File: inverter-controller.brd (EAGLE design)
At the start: 18.5 x 86.8 mm, 140 parts, among them IC1 STM32F334C8T6, IC2 SY7152ABC, IC3 LMV358MMX, IC4 LMV358MMX, IC5 SY7152ABC, J1 621006245821, J2 61300211121, X1 0289-9066**15EDGVC-3.81-02P-14, X2 0289-9066**15EDGVC-3.81-02P-14, X4 0289-9066**15EDGVC-3.81-02P-14, X6 1365-16, Y1 NX2016SA-32M

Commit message: Direnc ve kondansator kutuphaneleri degistirildi(silk sorunu nedeniyle).
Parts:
- removed C58: 100n, rcl:C0603
- removed LED10, LED7, LED9: (no value), adafruit:CHIPLED_0805
- removed R51, R52, R62, R63, R64: 33R, rcl:R0603
- removed R53, R54, R65, R66: 1k, rcl:R0603
- removed R55, R76: 470R, rcl:R0603
- removed R56: 220R, rcl:R0603
- removed R57: 1M, rcl:R0603
- removed R58: 200k, rcl:R0603
- removed R59: 10.5k, rcl:R0603
- removed R60, R61: 0R, rcl:R0603
- removed R71, R75: NC, rcl:R0603
- added C20: 10nF, rcl:C0603_ENKO
- added LED1, LED2, LED3: (no value), adafruit:CHIP-LED0805
- added R16: 220R, rcl:R0603_ENKO
- added R36, R37: 470R, rcl:R0603_ENKO
- added R38, R39, R47: 33R, rcl:R0603_ENKO
- added R40, R44: 1K, rcl:R0603_ENKO
- added R41: 1M, rcl:R0603_ENKO
- added R42: 200K, rcl:R0603_ENKO
- added R43: 10.5K, rcl:R0603_ENKO
- added R45, R46: 0R, rcl:R0603_ENKO
- C1, C2: value (none) -> 10pF; device rcl:C0603 -> rcl:C0603_ENKO
- C10, C13, C19, C37, C38, C47: value 100n -> 100nF; device rcl:C0603 -> rcl:C0603_ENKO
- C11: value 4.7u -> 4.7uF; device rcl:C0603 -> rcl:C0603_ENKO
- C12: value 1019-3366**CAP 0603 CER 10uF 16V %20 X5R -> 10uF; device rcl:C0603 -> rcl:C0603_ENKO
- C14, C3, C39, C48, C5, C52, C57: value 10n -> 10nF; device rcl:C0603 -> rcl:C0603_ENKO
- C15, C16, C54: value 10u -> 10uF; device rcl:C0805 -> rcl:C0603_ENKO
- C17, C22, C24, C26, C28, C30, C32, C34, C42, C45, C51: value 100n -> 10nF; device rcl:C0603 -> rcl:C0603_ENKO
- C18, C21, C23, C25, C27, C29, C31, C33, C35, C43, C46, C56: value 10n -> 100nF; device rcl:C0603 -> rcl:C0603_ENKO
- C36: value 100n -> 120pF; device rcl:C0603 -> rcl:C0603_ENKO
- C4: value 1u -> 1uF; device rcl:C0603 -> rcl:C0603_ENKO
- C40: value 120p -> 100nF; device rcl:C0603 -> rcl:C0603_ENKO
- C41, C44: value 120p -> 120pF; device rcl:C0603 -> rcl:C0603_ENKO
- C49, C55: value 100n -> 10uF; device rcl:C0603 -> rcl:C0603_ENKO
- C50: value 1019-3366**CAP 0603 CER 10uF 16V %20 X5R -> 100nF; device rcl:C0603 -> rcl:C0603_ENKO
- C53: value 10u -> 100nF; device rcl:C0805 -> rcl:C0603_ENKO
- C6, C8: value 100n -> 4.7uF; device rcl:C0603 -> rcl:C0603_ENKO
- C7, C9: value 4.7u -> 100nF; device rcl:C0603 -> rcl:C0603_ENKO
- R1, R32: value (none) -> 1K; device rcl:R0603 -> rcl:R0603_ENKO
- R10, R11, R12, R13, R14, R15, R17, R18, R19, R2, R20, R21, R22, R23, R24, R25, R26, R27, R28, R29, R30, R31, R4, R7, R8, R9: device rcl:R0603 -> rcl:R0603_ENKO
- R3: value 10k -> 10K; device rcl:R0603 -> rcl:R0603_ENKO
- R33, R34: value (none) -> 0R; device rcl:R0603 -> rcl:R0603_ENKO
- R35: value (none) -> 33R; device rcl:R0603 -> rcl:R0603_ENKO
- R48, R49: value 0R -> 33R; device rcl:R0603 -> rcl:R0603_ENKO
- R5: value 200k -> 200K; device rcl:R0603 -> rcl:R0603_ENKO
- R50: value 33R -> 1K; device rcl:R0603 -> rcl:R0603_ENKO
- R6: value 10.5k -> 10.5K; device rcl:R0603 -> rcl:R0603_ENKO
- moved R50 653.0 mm to (-144.2, -544.9)
- moved C57 652.1 mm to (-144.2, -554.9)
- moved R49 648.8 mm to (-144.2, -539.9)
- moved C56 647.4 mm to (-144.2, -549.9)
- moved R48 644.7 mm to (-144.2, -534.9)
- moved C55 604.1 mm to (-138.1, -510.0)
- moved C52 592.6 mm to (-138.1, -495.0)
- moved C54 580.2 mm to (-138.1, -505.0)
- moved C53 576.0 mm to (-138.1, -500.0)
- moved C51 570.0 mm to (-138.1, -475.0)
- moved C49 560.8 mm to (-138.1, -465.1)
- moved C48 558.0 mm to (-138.1, -460.1)
- moved R35 555.8 mm to (-138.1, -435.1)
- moved R32 552.0 mm to (-131.9, -430.1)
- moved C47 551.7 mm to (-138.1, -455.1)
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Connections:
- removed net HRTIM1_CHA1: IC1.29, R17.1
- removed net HRTIM1_CHA2: IC1.30, R18.1
- removed net HRTIM1_CHB1: IC1.31, R19.1
- removed net HRTIM1_CHB2: IC1.32, R20.1
- removed net N$39: LED9.A, R56.2
- removed net N$48: C12.1, C13.1, C14.1, IC2.5, L4.1, R71.2
- removed net N$51: C50.1, C51.1, C52.1, IC5.5, L1.1, R75.2
- new net N$22: LED1.A, R16.2
- net +12V/1: now also R32.1, R33.2, R34.2, R5.1; no longer R48.2, R49.2, R5.2, R54.1
- net +12V/2: now also C52.1, R42.1, R44.1, R45.2, R46.2; no longer C56.1, R58.2, R60.2, R61.2, R66.1
- net +3V3: now also C12.1, C13.1, C14.1, C46.1, C49.1, C50.1, C51.1, C6.1, C7.1, IC2.5, IC5.5, L1.1, L4.1, R16.1, R18.1, R36.1, R37.1; no longer C47.1, C6.2, C7.2, R33.1, R55.1, R56.1, R71.1, R75.1, R76.1
- net FAN2_EN: now also R41.2; no longer R57.2
- net G11_PWM: now also IC1.29; no longer R17.2
- net G12_PWM: now also IC1.30; no longer R18.2
- net G13_PWM: now also IC1.31; no longer R19.2
- net G14_PWM: now also IC1.32; no longer R20.2
- net GND: now also C19.1, C20.2, C40.2, C6.2, C7.2, LED1.C, LED2.C, LED3.C, R19.2, R24.2, R29.2, R35.2, R38.2, R39.2, R41.1, R43.2, R47.2, R48.2, R49.2, R6.2, R7.2; no longer C19.2, C36.2, C58.2, C6.1, C7.1, LED10.C, LED7.C, LED9.C, R24.1, R29.1, R34.1, R50.2, R51.2, R52.2, R57.1, R59.1, R6.1, R62.2, R63.2, R64.2, R7.1
- net IA: now also C26.1, R17.1; no longer C28.1, R21.1
- net IB: now also C30.1, R22.1; no longer C32.1, R27.1
- net IIN_SENS: now also R8.2; no longer R8.1
- net I_FAN: now also C47.1, C56.1, R40.2, R50.2; no longer C49.1, C58.1, R53.2, R65.2
- net I_IN: now also C34.1, R27.1, R8.1; no longer C36.1, R32.1, R8.2
- net N$1: now also C36.2, R20.1, R21.2; no longer C40.2, R22.2, R25.1
- net N$10: now also R35.1, R38.1, R39.1, R40.1; no longer R50.1, R51.1, R52.1, R53.1
- net N$13: now also R20.2; no longer R25.2
- net N$14: now also C42.1, R26.2; no longer C43.1, R30.2
- net N$15: now also R18.2, R19.1; no longer R23.2, R24.2
- net N$16: now also R22.2, R25.1; no longer R26.1, R27.2
- net N$17: now also R27.2, R30.1; no longer R31.1, R32.2
- net N$18: now also C40.1, R23.2, R24.1; no longer C42.1, R28.2, R29.2
- net N$19: now also R25.2, R26.1; no longer R26.2, R30.1
- net N$20: now also C45.1, R31.2; no longer C46.1, R35.2
- net N$21: now also C43.1, R28.2, R29.1; no longer C45.1, R33.2, R34.2
- net N$23: now also R30.2, R31.1; no longer R31.2, R35.1
- net N$34: now also R33.1, R34.1; no longer R48.1, R49.1
- net N$35: now also R36.2; no longer R76.2
- net N$40: now also R42.2, R43.1; no longer R58.1, R59.2
- net N$41: now also R45.1, R46.1; no longer R60.1, R61.1
- net N$42: now also R47.1, R48.1, R49.1, R50.1; no longer R62.1, R63.1, R64.1, R65.1
- net N$43: now also LED3.A, R44.2; no longer LED10.A, R66.2
- net N$47: now also R37.2; no longer R55.2
- net N$7: now also C36.1, R17.2, R21.1; no longer C40.1, R21.2, R22.1
- net N$8: now also R5.2, R6.1; no longer R5.1, R6.2
- net N$9: now also LED2.A, R32.2; no longer LED7.A, R54.2
- net NTC1: now also C19.2, R7.1; no longer C19.1, R7.2
- net VA: now also C24.1; no longer C26.1
- net VB: now also C28.1; no longer C30.1
- net VIN_1: now also C20.1; no longer C22.1
- net VIN_2: now also C32.1; no longer C34.1
- net VOUT: now also C22.1; no longer C24.1
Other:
- board size 18.5 x 86.8 mm -> 52 x 37.6 mm

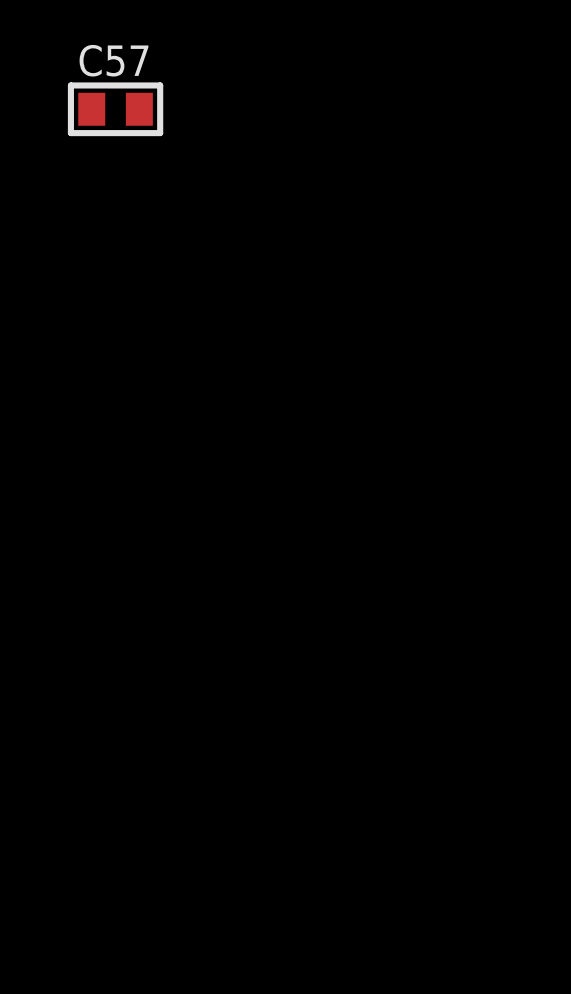
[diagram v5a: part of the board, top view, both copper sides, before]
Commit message: Akim olcumleri icin gerilim bolucu direncler eklendi.
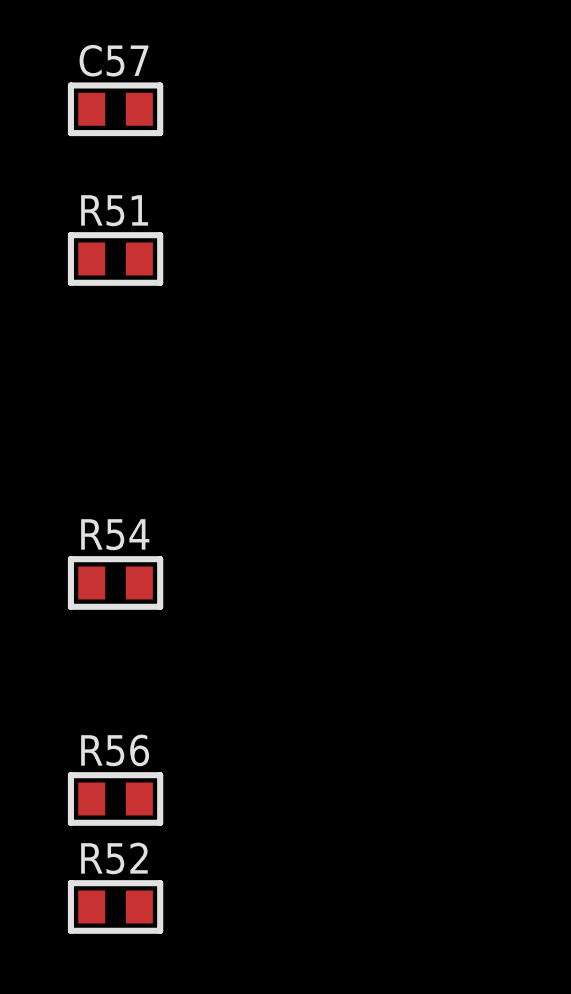
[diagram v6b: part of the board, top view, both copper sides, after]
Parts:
- added R51, R52, R54, R56: (no value), rcl:R0603_ENKO
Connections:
- net GND: now also R51.1, R52.1, R54.1, R56.1
- net IA: now also R54.2
- net IB: now also R56.2
- net I_IN: now also R52.2
- net VIN_1: now also R51.2
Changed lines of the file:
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@@
 <attribute name="VALUE" x="-145.5" y="-556.775" size="0.8128" layer="27" ratio="10"/>
+</element>
+<element name="R51" library="rcl" library_urn="urn:adsk.eagle:library:26637914" package="R0603_ENKO" package3d_urn="urn:adsk.eagle:package:26638826/1" value="" x="-144.23" y="-559.86" smashed="yes">
+<attribute name="NAME" x="-145.5" y="-558.7487" size="1.016" layer="25" ratio="18"/>
+<attribute name="VALUE" x="-145.5" y="-561.765" size="0.8128" layer="27" ratio="10"/>
+</element>
+<element name="R54" library="rcl" library_urn="urn:adsk.eagle:library:26637914" package="R0603_ENKO" package3d_urn="urn:adsk.eagle:package:26638826/1" value="" x="-144.23" y="-570.66" smashed="yes">
+<attribute name="NAME" x="-145.5" y="-569.5487" size="1.016" layer="25" ratio="18"/>
+<attribute name="VALUE" x="-145.5" y="-572.565" size="0.8128" layer="27" ratio="10"/>
+</element>
+<element name="R56" library="rcl" library_urn="urn:adsk.eagle:library:26637914" package="R0603_ENKO" package3d_urn="urn:adsk.eagle:package:26638826/1" value="" x="-144.23" y="-577.86" smashed="yes">
+<attribute name="NAME" x="-145.5" y="-576.7487" size="1.016" layer="25" ratio="18"/>
+<attribute name="VALUE" x="-145.5" y="-579.765" size="0.8128" layer="27" ratio="10"/>
+</element>
+<element name="R52" library="rcl" library_urn="urn:adsk.eagle:library:26637914" package="R0603_ENKO" package3d_urn="urn:adsk.eagle:package:26638826/1" value="" x="-144.23" y="-581.46" smashed="yes">
+<attribute name="NAME" x="-145.5" y="-580.3487" size="1.016" layer="25" ratio="18"/>
+<attribute name="VALUE" x="-145.5" y="-583.365" size="0.8128" layer="27" ratio="10"/>
 </element>
 </elements>
@@
 <contactref element="R11" pad="2"/>
 <contactref element="R17" pad="1"/>
+<contactref element="R54" pad="2"/>
 <wire x1="-126.5738" y1="-87.02" x2="-126.5738" y2="-92.01" width="0" layer="19" extent="1-1"/>
 <wire x1="-124.9862" y1="-134.14" x2="-126.5738" y2="-92.01" width="0" layer="19" extent="1-1"/>
 <wire x1="-132.7238" y1="-249.16" x2="-124.9862" y2="-134.14" width="0" layer="19" extent="1-1"/>
 <wire x1="36.26" y1="41.148" x2="-126.5738" y2="-87.02" width="0" layer="19" extent="1-16"/>
+<wire x1="-143.4362" y1="-570.66" x2="-132.7238" y2="-249.16" width="0" layer="19" extent="1-1"/>
 </signal>
 <signal name="IB">
@@
 <contactref element="R9" pad="2"/>
 <contactref element="R22" pad="1"/>
+<contactref element="R56" pad="2"/>
 <wire x1="-126.5738" y1="-111.97" x2="-124.9862" y2="-126.94" width="0" layer="19" extent="1-1"/>
 <wire x1="-126.5738" y1="-106.98" x2="-126.5738" y2="-111.97" width="0" layer="19" extent="1-1"/>
 <wire x1="-132.7238" y1="-287.12" x2="-124.9862" y2="-126.94" width="0" layer="19" extent="1-1"/>
 <wire x1="39.748" y1="39.66" x2="-126.5738" y2="-106.98" width="0" layer="19" extent="1-16"/>
+<wire x1="-143.4362" y1="-577.86" x2="-132.7238" y2="-287.12" width="0" layer="19" extent="1-1"/>
 </signal>
 <signal name="VIN_1">
@@
 <contactref element="C21" pad="1"/>
 <contactref element="R14" pad="2"/>
+<contactref element="R51" pad="2"/>
+<wire x1="-124.9862" y1="-144.94" x2="-143.4362" y2="-559.86" width="0" layer="19" extent="1-1"/>
+<wire x1="-126.5738" y1="-67.63" x2="-124.9862" y2="-144.94" width="0" layer="19" extent="1-1"/>
 <wire x1="-126.5738" y1="-64.03" x2="-126.5738" y2="-67.63" width="0" layer="19" extent="1-1"/>
-<wire x1="-124.9862" y1="-144.94" x2="-126.5738" y2="-67.63" width="0" layer="19" extent="1-1"/>
 <wire x1="39.748" y1="38.66" x2="-126.5738" y2="-64.03" width="0" layer="19" extent="1-16"/>
 </signal>
@@
 <contactref element="C35" pad="1"/>
 <contactref element="R27" pad="1"/>
+<contactref element="R52" pad="2"/>
+<wire x1="-132.7238" y1="-320.09" x2="-143.4362" y2="-581.46" width="0" layer="19" extent="1-1"/>
 <wire x1="-126.5738" y1="-165.72" x2="-132.7238" y2="-320.09" width="0" layer="19" extent="1-1"/>
 <wire x1="-126.5738" y1="-160.73" x2="-126.5738" y2="-165.72" width="0" layer="19" extent="1-1"/>
@@
 <contactref element="C56" pad="2"/>
 <contactref element="C57" pad="2"/>
+<contactref element="R51" pad="1"/>
+<contactref element="R54" pad="1"/>
+<contactref element="R56" pad="1"/>
+<contactref element="R52" pad="1"/>
 <wire x1="-131.1362" y1="-371.63" x2="-131.1362" y2="-376.62" width="0" layer="19" extent="1-1"/>
 <wire x1="-131.1362" y1="-366.64" x2="-131.1362" y2="-371.63" width="0" layer="19" extent="1-1"/>
@@
 <wire x1="-143.4362" y1="-549.88" x2="-143.4362" y2="-539.9" width="0" layer="19" extent="1-1"/>
 <wire x1="-143.4362" y1="-554.87" x2="-143.4362" y2="-549.88" width="0" layer="19" extent="1-1"/>
+<wire x1="-145.0238" y1="-559.86" x2="-143.4362" y2="-554.87" width="0" layer="19" extent="1-1"/>
+<wire x1="-145.0238" y1="-570.66" x2="-145.0238" y2="-559.86" width="0" layer="19" extent="1-1"/>
+<wire x1="-145.0238" y1="-577.86" x2="-145.0238" y2="-570.66" width="0" layer="19" extent="1-1"/>
+<wire x1="-145.0238" y1="-581.46" x2="-145.0238" y2="-577.86" width="0" layer="19" extent="1-1"/>
 <wire x1="-124.9862" y1="-165.72" x2="-132.7238" y2="-184.29" width="0" layer="19" extent="1-1"/>
 <wire x1="-124.9862" y1="-160.73" x2="-124.9862" y2="-165.72" width="0" layer="19" extent="1-1"/>

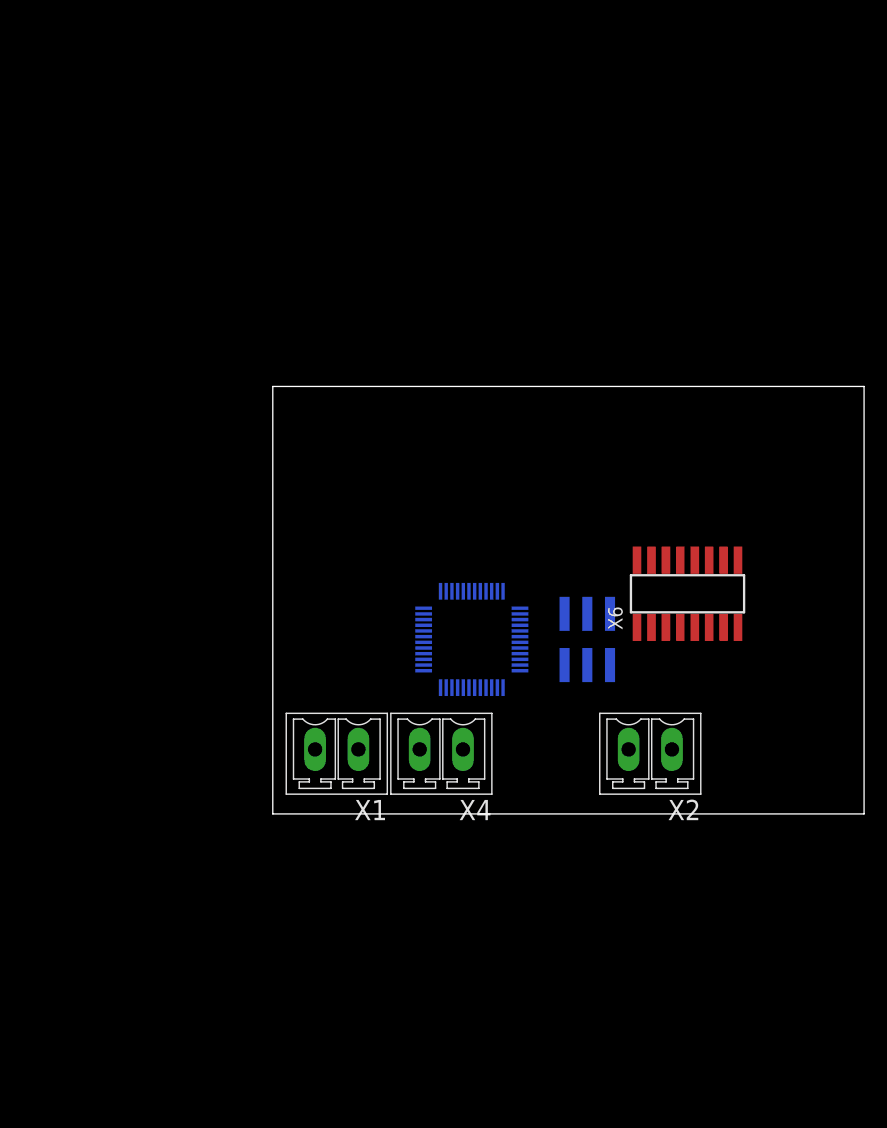
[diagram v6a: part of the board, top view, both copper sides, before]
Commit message: Kart boyutu ayarlandi, baglanti soketi yerlesimi yapildi.
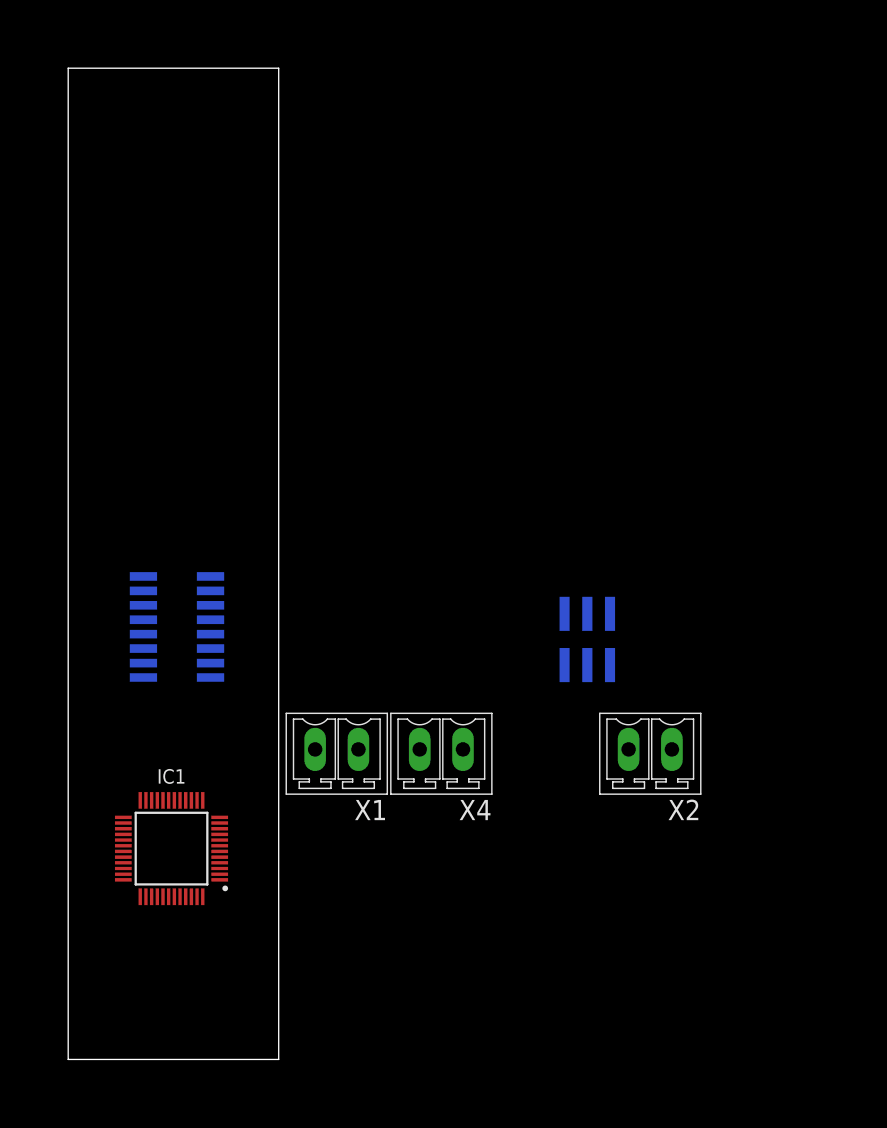
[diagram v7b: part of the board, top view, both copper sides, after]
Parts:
- moved X6 45.0 mm to (9.57, 38.0), flipped to the bottom, turned to 90 degrees
- moved IC1 32.2 mm to (9.09, 18.5), flipped to the top
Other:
- board size 52 x 37.6 mm -> 18.5 x 87.2 mm

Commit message: Fan beslemelerinden bir tanesi silindi.
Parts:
- removed C49, C54, C55: 10uF, rcl:C0603_ENKO
- removed C50, C53, C56: 100nF, rcl:C0603_ENKO
- removed C51, C52, C57: 10nF, rcl:C0603_ENKO
- removed D8: 1119-3055, Diode:DIOM5226X290N
- removed IC5: SY7152ABC, SY7152ABC:SOT95P285X140-6N
- removed L1: 1319-4102**INDUCTOR POWER 22UH 4X4X1.8MM SMD, wuerth-elektronik:WE-PD2_S
- removed LED3: (no value), adafruit:CHIP-LED0805
- removed R41: 1M, rcl:R0603_ENKO
- removed R42: 200K, rcl:R0603_ENKO
- removed R43: 10.5K, rcl:R0603_ENKO
- removed R44, R50: 1K, rcl:R0603_ENKO
- removed R45, R46: 0R, rcl:R0603_ENKO
- removed R47, R48, R49: 33R, rcl:R0603_ENKO
- removed X4: 0289-9066**15EDGVC-3.81-02P-14, con-phoenix-381_l:MCV2
- moved J1 55.1 mm to (13.8, 81.9), flipped to the top
- moved X1 51.4 mm to (4.24, 74.9), turned to 90 degrees
- moved X2 43.7 mm to (13.7, 4.74)
- moved IC1 39.0 mm to (9.41, 57.5), flipped to the bottom
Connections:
- removed net +12V/2: C52.1, C53.1, C54.1, C55.1, D8.1, R42.1, R44.1, R45.2, R46.2
- removed net N$36: D8.2, IC5.1, L1.2
- removed net N$40: IC5.3, R42.2, R43.1
- removed net N$41: R45.1, R46.1, X4.1
- removed net N$42: R47.1, R48.1, R49.1, R50.1, X4.2
- removed net N$43: LED3.A, R44.2
- net +3V3: no longer C49.1, C50.1, C51.1, IC5.5, L1.1
- net FAN2_EN: no longer IC5.4, R41.2
- net GND: no longer C49.2, C50.2, C51.2, C52.2, C53.2, C54.2, C55.2, C56.2, C57.2, IC5.2, LED3.C, R41.1, R43.2, R47.2, R48.2, R49.2
- net I_FAN: no longer C56.1, C57.1, R50.2
